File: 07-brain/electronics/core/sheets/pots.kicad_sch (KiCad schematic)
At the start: 7 parts, among them U1 74HC4051

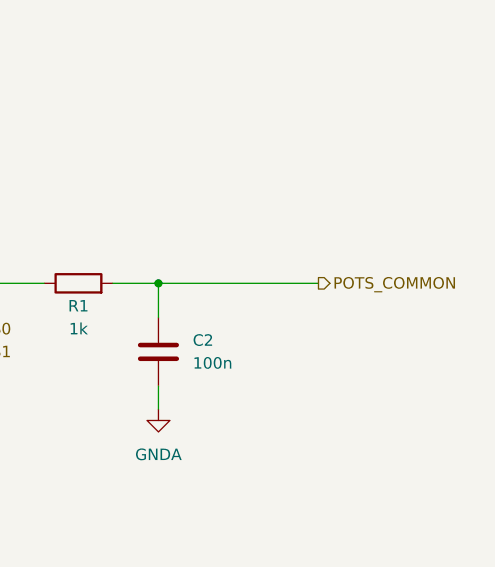
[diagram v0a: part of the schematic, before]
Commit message: Added LED component to Brain (untested)
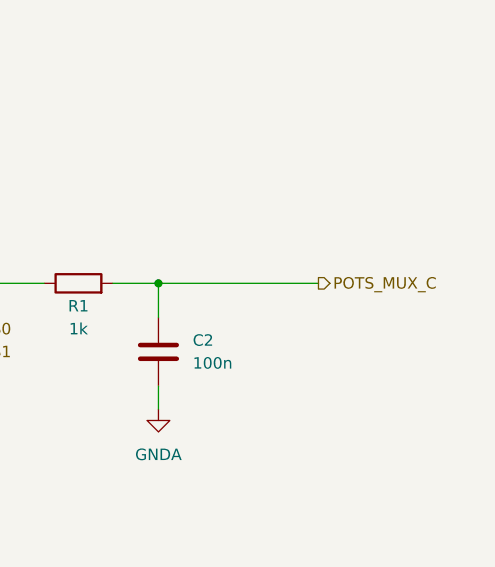
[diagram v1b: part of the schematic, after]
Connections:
- net POTS_COMMON renamed POTS_MUX_C
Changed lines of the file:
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@@
 		)
 	)
-	(hierarchical_label "POTS_COMMON"
+	(hierarchical_label "POTS_MUX_C"
 		(shape output)
 		(at 208.28 68.58 0)

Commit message: Updated Brain schematics
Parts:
- removed RV2, RV3: R_Potentiometer, symbol Device:R_Potentiometer
- #RV1: renamed from RV1; value R_Potentiometer -> 100k
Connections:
- net POT_3: now reaches U1.15 (A2)
- net at #RV1.2: no longer U1.13 (A0)
- net POT_2: now reaches U1.14 (A1)
- new net POT_1: U1.13 (A0)

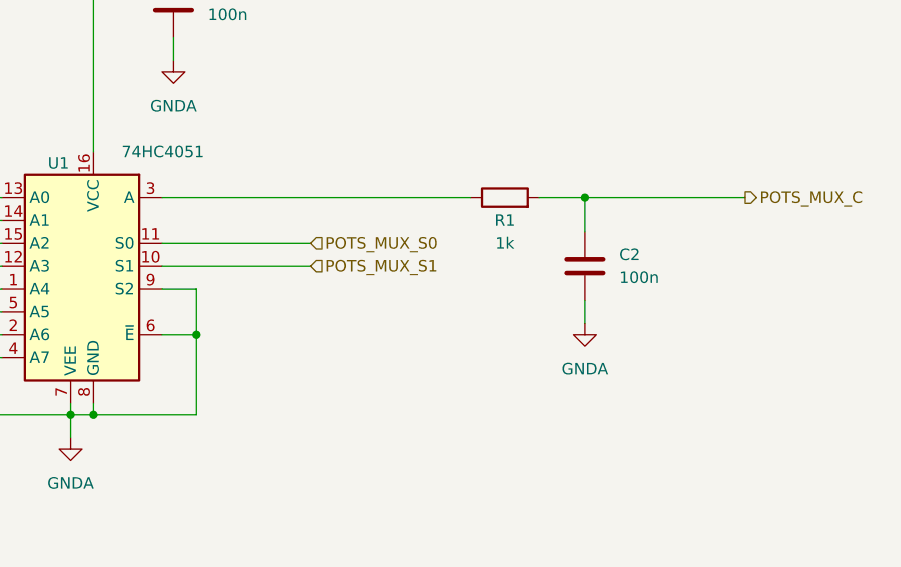
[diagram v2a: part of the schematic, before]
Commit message: Added pot mux logic
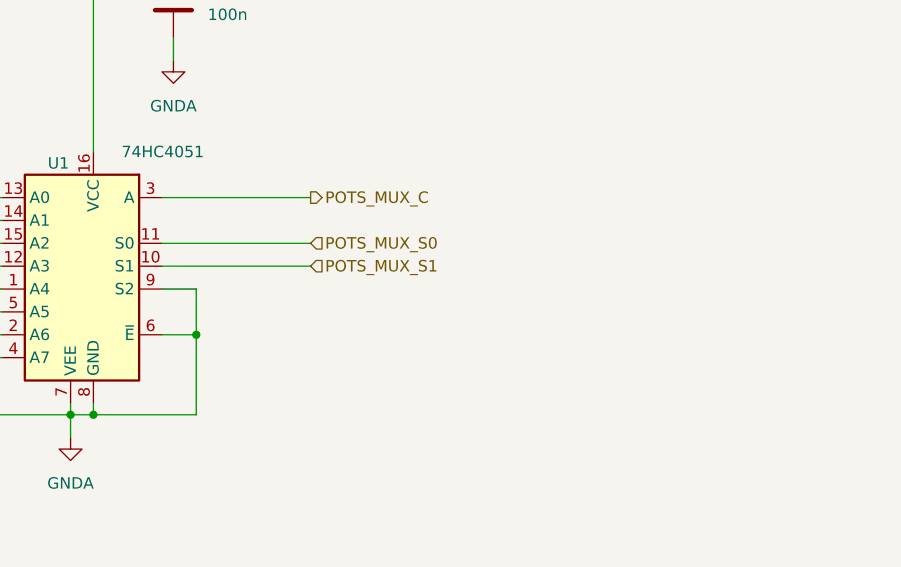
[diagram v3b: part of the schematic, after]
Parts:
- removed C2: 100n, Capacitor_SMD:C_0603_1608Metric, symbol Device:C
- removed R1: 1k, Resistor_SMD:R_0603_1608Metric, symbol Device:R
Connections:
- net POTS_MUX_C: now also U1.3 (A)

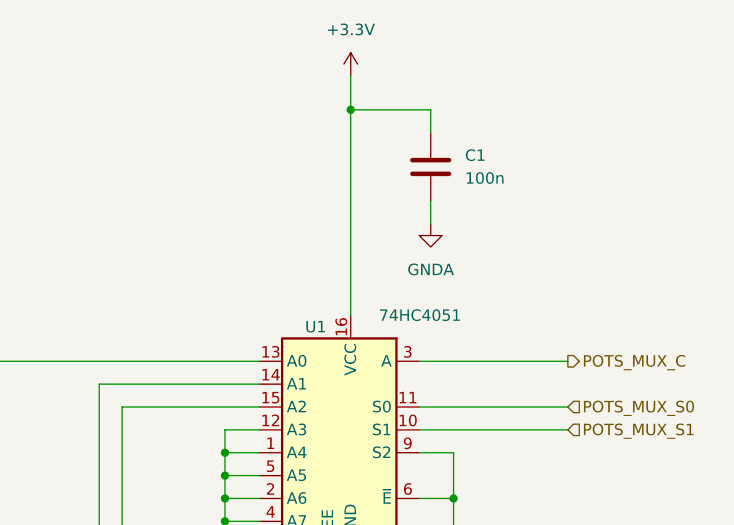
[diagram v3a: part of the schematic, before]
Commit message: Audio/CV out BrainSDK tested/working
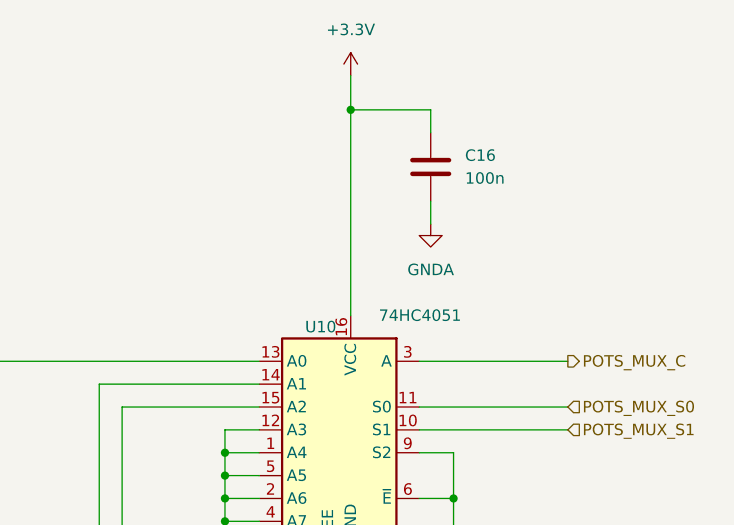
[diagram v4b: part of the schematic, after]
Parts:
- renumbered C1 to C16, U1 to U10
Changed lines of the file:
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@@
 		(dnp no)
 		(fields_autoplaced yes)
-		(property "Reference" "C1"
+		(property "Reference" "C16"
 			(at 148.59 45.72 0)
 			(effects
@@
 			(project "brain-core"
 				(path "/8e2e31f3-eed5-4de1-966c-f4162758c735/6d9ed0a4-9ccf-4f42-8434-45714a6fdbff"
-					(reference "C1")
+					(reference "C16")
 					(unit 1)
 				)
@@
 		(dnp no)
 		(fields_autoplaced yes)
-		(property "Reference" "#PWR01"
+		(property "Reference" "#PWR065"
 			(at 67.31 66.04 0)
 			(effects
@@
 			(project ""
 				(path "/8e2e31f3-eed5-4de1-966c-f4162758c735/6d9ed0a4-9ccf-4f42-8434-45714a6fdbff"
-					(reference "#PWR01")
+					(reference "#PWR065")
 					(unit 1)
 				)
@@
 		(on_board yes)
 		(dnp no)
-		(property "Reference" "U1"
+		(property "Reference" "U10"
 			(at 130.81 64.77 0)
 			(effects
@@
 			(project ""
 				(path "/8e2e31f3-eed5-4de1-966c-f4162758c735/6d9ed0a4-9ccf-4f42-8434-45714a6fdbff"
-					(reference "U1")
+					(reference "U10")
 					(unit 1)
 				)
@@
 		(dnp no)
 		(fields_autoplaced yes)
-		(property "Reference" "#PWR02"
+		(property "Reference" "#PWR069"
 			(at 144.78 59.69 0)
 			(effects
@@
 			(project "brain-core"
 				(path "/8e2e31f3-eed5-4de1-966c-f4162758c735/6d9ed0a4-9ccf-4f42-8434-45714a6fdbff"
-					(reference "#PWR02")
+					(reference "#PWR069")
 					(unit 1)
 				)
@@
 		(dnp no)
 		(fields_autoplaced yes)
-		(property "Reference" "#PWR032"
+		(property "Reference" "#PWR067"
 			(at 133.35 101.6 0)
 			(effects
@@
 			(project "brain-core"
 				(path "/8e2e31f3-eed5-4de1-966c-f4162758c735/6d9ed0a4-9ccf-4f42-8434-45714a6fdbff"
-					(reference "#PWR032")
+					(reference "#PWR067")
 					(unit 1)
 				)
@@
 		(dnp no)
 		(fields_autoplaced yes)
-		(property "Reference" "#PWR034"
+		(property "Reference" "#PWR068"
 			(at 135.89 40.64 0)
 			(effects
@@
 			(project ""
 				(path "/8e2e31f3-eed5-4de1-966c-f4162758c735/6d9ed0a4-9ccf-4f42-8434-45714a6fdbff"
-					(reference "#PWR034")
+					(reference "#PWR068")
 					(unit 1)
 				)
@@
 		(dnp no)
 		(fields_autoplaced yes)
-		(property "Reference" "#PWR033"
+		(property "Reference" "#PWR066"
 			(at 67.31 81.28 0)
 			(effects
@@
 			(project "brain-core"
 				(path "/8e2e31f3-eed5-4de1-966c-f4162758c735/6d9ed0a4-9ccf-4f42-8434-45714a6fdbff"
-					(reference "#PWR033")
-					(unit 1)
-				)
+					(reference "#PWR066")
+					(unit 1)
+				)

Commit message: Design Brain/Core PCB
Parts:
- U10: footprint (none) -> Package_SO:SOIC-16_3.9x9.9mm_P1.27mm
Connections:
- no-connect marks 0 -> 1
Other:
- note added: "Sample"
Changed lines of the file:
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@@
 	(generator_version "9.0")
 	(paper "A4")
+	(rectangle
+		(start 57.15 50.8)
+		(end 77.47 86.36)
+		(stroke
+			(width 0)
+			(type default)
+		)
+		(fill
+			(type none)
+		)
+	)
+	(text "Sample"
+		(exclude_from_sim no)
+		(at 59.69 49.53 0)
+		(effects
+			(font
+				(size 1.27 1.27)
+			)
+		)
+	)
 	(junction
 		(at 133.35 92.71)
@@
 		(diameter 0)
 		(color 0 0 0 0)
+	)
+	(no_connect
+		(at 71.12 68.58)
 	)
 	(wire
@@
 			)
 		)
-		(property "Footprint" ""
+		(property "Footprint" "Package_SO:SOIC-16_3.9x9.9mm_P1.27mm"
 			(at 135.89 86.36 0)
 			(effects

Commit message: Brain PCB WIP
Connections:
- net GNDA renamed GND
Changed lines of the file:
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@@
 	(wire
 		(pts
-			(xy 133.35 95.25) (xy 133.35 92.71)
+			(xy 133.35 92.71) (xy 133.35 96.52)
 		)
 		(stroke
@@
 	)
 	(symbol
-		(lib_id "power:GNDA")
-		(at 144.78 53.34 0)
+		(lib_id "power:GND")
+		(at 67.31 74.93 0)
 		(unit 1)
 		(exclude_from_sim no)
@@
 		(dnp no)
 		(fields_autoplaced yes)
-		(property "Reference" "#PWR069"
-			(at 144.78 59.69 0)
-			(effects
-				(font
-					(size 1.27 1.27)
-				)
-				(hide yes)
-			)
-		)
-		(property "Value" "GNDA"
-			(at 144.78 58.42 0)
+		(property "Reference" "#PWR059"
+			(at 67.31 81.28 0)
+			(effects
+				(font
+					(size 1.27 1.27)
+				)
+				(hide yes)
+			)
+		)
+		(property "Value" "GND"
+			(at 67.31 80.01 0)
 			(effects
 				(font
@@
 		)
 		(property "Footprint" ""
-			(at 144.78 53.34 0)
+			(at 67.31 74.93 0)
 			(effects
 				(font
@@
 		)
 		(property "Datasheet" ""
-			(at 144.78 53.34 0)
-			(effects
-				(font
-					(size 1.27 1.27)
-				)
-				(hide yes)
-			)
-		)
-		(property "Description" "Power symbol creates a global label with name \"GNDA\" , analog ground"
-			(at 144.78 53.34 0)
+			(at 67.31 74.93 0)
+			(effects
+				(font
+					(size 1.27 1.27)
+				)
+				(hide yes)
+			)
+		)
+		(property "Description" "Power symbol creates a global label with name \"GND\" , ground"
+			(at 67.31 74.93 0)
 			(effects
 				(font
@@
 			(project "brain-core"
 				(path "/8e2e31f3-eed5-4de1-966c-f4162758c735/6d9ed0a4-9ccf-4f42-8434-45714a6fdbff"
-					(reference "#PWR069")
+					(reference "#PWR059")
 					(unit 1)
 				)
@@
 	)
 	(symbol
-		(lib_id "power:GNDA")
-		(at 133.35 95.25 0)
+		(lib_id "power:GND")
+		(at 133.35 96.52 0)
 		(unit 1)
 		(exclude_from_sim no)
@@
 		(dnp no)
 		(fields_autoplaced yes)
-		(property "Reference" "#PWR067"
+		(property "Reference" "#PWR058"
+			(at 133.35 102.87 0)
+			(effects
+				(font
+					(size 1.27 1.27)
+				)
+				(hide yes)
+			)
+		)
+		(property "Value" "GND"
 			(at 133.35 101.6 0)
 			(effects
@@
 					(size 1.27 1.27)
 				)
-				(hide yes)
-			)
-		)
-		(property "Value" "GNDA"
-			(at 133.35 100.33 0)
-			(effects
-				(font
-					(size 1.27 1.27)
-				)
 			)
 		)
 		(property "Footprint" ""
-			(at 133.35 95.25 0)
+			(at 133.35 96.52 0)
 			(effects
 				(font
@@
 		)
 		(property "Datasheet" ""
-			(at 133.35 95.25 0)
-			(effects
-				(font
-					(size 1.27 1.27)
-				)
-				(hide yes)
-			)
-		)
-		(property "Description" "Power symbol creates a global label with name \"GNDA\" , analog ground"
-			(at 133.35 95.25 0)
+			(at 133.35 96.52 0)
+			(effects
+				(font
+					(size 1.27 1.27)
+				)
+				(hide yes)
+			)
+		)
+		(property "Description" "Power symbol creates a global label with name \"GND\" , ground"
+			(at 133.35 96.52 0)
 			(effects
 				(font
@@
 			(project "brain-core"
 				(path "/8e2e31f3-eed5-4de1-966c-f4162758c735/6d9ed0a4-9ccf-4f42-8434-45714a6fdbff"
-					(reference "#PWR067")
+					(reference "#PWR058")
 					(unit 1)
 				)
@@
 	)
 	(symbol
-		(lib_id "power:GNDA")
-		(at 67.31 74.93 0)
+		(lib_id "power:GND")
+		(at 144.78 53.34 0)
 		(unit 1)
 		(exclude_from_sim no)
@@
 		(dnp no)
 		(fields_autoplaced yes)
-		(property "Reference" "#PWR066"
-			(at 67.31 81.28 0)
-			(effects
-				(font
-					(size 1.27 1.27)
-				)
-				(hide yes)
-			)
-		)
-		(property "Value" "GNDA"
-			(at 67.31 80.01 0)
+		(property "Reference" "#PWR060"
+			(at 144.78 59.69 0)
+			(effects
+				(font
+					(size 1.27 1.27)
+				)
+				(hide yes)
+			)
+		)
+		(property "Value" "GND"
+			(at 144.78 58.42 0)
 			(effects
 				(font
@@
 		)
 		(property "Footprint" ""
-			(at 67.31 74.93 0)
+			(at 144.78 53.34 0)
 			(effects
 				(font
@@
 		)
 		(property "Datasheet" ""
-			(at 67.31 74.93 0)
-			(effects
-				(font
-					(size 1.27 1.27)
-				)
-				(hide yes)
-			)
-		)
-		(property "Description" "Power symbol creates a global label with name \"GNDA\" , analog ground"
-			(at 67.31 74.93 0)
+			(at 144.78 53.34 0)
+			(effects
+				(font
+					(size 1.27 1.27)
+				)
+				(hide yes)
+			)
+		)
+		(property "Description" "Power symbol creates a global label with name \"GND\" , ground"
+			(at 144.78 53.34 0)
 			(effects
 				(font
@@
 			(project "brain-core"
 				(path "/8e2e31f3-eed5-4de1-966c-f4162758c735/6d9ed0a4-9ccf-4f42-8434-45714a6fdbff"
-					(reference "#PWR066")
+					(reference "#PWR060")
 					(unit 1)
 				)

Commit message: Brain electronics prod ready
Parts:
- C16: CHECKED (none) -> YES
- U10: CHECKED (none) -> YES; LCSC (none) -> C9386; Vendor (none) -> JLCPCB
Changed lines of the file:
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@@
+			)
+		)
+		(property "CHECKED" "YES"
+			(at 144.78 46.99 0)
+			(effects
+				(font
+					(size 1.27 1.27)
+				)
+				(hide yes)
 			)
 		)
@@
 			(at 135.89 76.2 0)
 			(effects
+				(font
+					(size 1.27 1.27)
+				)
+				(hide yes)
+			)
+		)
+		(property "LCSC" "C9386"
+			(at 135.89 76.2 0)
+			(effects
+				(font
+					(size 1.27 1.27)
+				)
+				(hide yes)
+			)
+		)
+		(property "Vendor" "JLCPCB"
+			(at 135.89 76.2 0)
+			(effects
+				(font
+					(size 1.27 1.27)
+				)
+				(hide yes)
+			)
+		)
+		(property "CHECKED" "YES"
+			(at 135.89 76.2 0)
+			(effects
